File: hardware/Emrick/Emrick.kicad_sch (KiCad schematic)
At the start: 85 parts, among them J1 LED_STRIP_CONNECTOR, J2 UFL, J3 Conn_02x05_Odd_Even, J4 BATT_CONN, P1 USB_C_Plug_USB2.0, Q1 Q_NPN_DGS, Q2 Q_NPN_DGS, Q3 Q_NPN_DGS, SW1 SW_SPST, SW2 SW_MEC_5E (RESET)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

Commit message: some work on pcb and schematic
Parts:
- added C13: ?, Capacitor_SMD:C_0402_1005Metric, symbol Device:C
- added L9: ?, Inductor_SMD:L_0402_1005Metric, symbol Device:L
- C12: value 100pF -> ?
- SW1: footprint Connector_PinHeader_2.54mm:PinHeader_1x03_P2.54mm_Vertical -> switch:SW-TH_3P-P4.70_L11.1-W12.7
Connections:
- net GND: now also C13.2, L9.2
- net at C17.1, L6.2: now also C13.1, L9.1
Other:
- note added: "C17, C13, L9, L6 for antenna matching"
- moved on the sheet: AE1, C17
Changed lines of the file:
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@@
   (junction (at 130.81 93.98) (diameter 0) (color 0 0 0 0)
   )
+  (junction (at 311.15 118.11) (diameter 0) (color 0 0 0 0)
+  )
   (junction (at 118.11 93.98) (diameter 0) (color 0 0 0 0)
   )
@@
   (junction (at 240.03 121.92) (diameter 0) (color 0 0 0 0)
   )
+  (junction (at 320.04 118.11) (diameter 0) (color 0 0 0 0)
+  )
   (junction (at 232.41 114.3) (diameter 0) (color 0 0 0 0)
   )
@@
     (stroke (width 0) (type default) (color 0 0 0 0))
   )
+  (wire (pts (xy 320.04 118.11) (xy 322.58 118.11))
+    (stroke (width 0) (type default) (color 0 0 0 0))
+  )
   (wire (pts (xy 153.67 228.6) (xy 156.21 228.6))
     (stroke (width 0) (type default) (color 0 0 0 0))
@@
     (stroke (width 0) (type default) (color 0 0 0 0))
   )
+  (wire (pts (xy 320.04 121.92) (xy 320.04 118.11))
+    (stroke (width 0) (type default) (color 0 0 0 0))
+  )
   (wire (pts (xy 377.19 220.98) (xy 377.19 222.25))
     (stroke (width 0) (type default) (color 0 0 0 0))
@@
     (stroke (width 0) (type default) (color 0 0 0 0))
   )
+  (wire (pts (xy 311.15 121.92) (xy 311.15 118.11))
+    (stroke (width 0) (type default) (color 0 0 0 0))
+  )
   (wire (pts (xy 153.67 102.87) (xy 153.67 104.14))
     (stroke (width 0) (type default) (color 0 0 0 0))
@@
     (stroke (width 0) (type default) (color 0 0 0 0))
   )
-  (wire (pts (xy 308.61 118.11) (xy 313.69 118.11))
+  (wire (pts (xy 308.61 118.11) (xy 311.15 118.11))
     (stroke (width 0) (type default) (color 0 0 0 0))
   )
@@
     (stroke (width 0) (type default) (color 0 0 0 0))
   )
+  (wire (pts (xy 311.15 118.11) (xy 320.04 118.11))
+    (stroke (width 0) (type default) (color 0 0 0 0))
+  )
   (wire (pts (xy 365.76 215.9) (xy 365.76 219.71))
     (stroke (width 0) (type default) (color 0 0 0 0))
@@
     (stroke (width 0) (type default) (color 0 0 0 0))
   )
-  (wire (pts (xy 321.31 118.11) (xy 330.2 118.11))
+  (wire (pts (xy 330.2 118.11) (xy 339.09 118.11))
     (stroke (width 0) (type default) (color 0 0 0 0))
   )
@@
     (effects (font (size 2 2)) (justify left bottom))
   )
+  (text "C17, C13, L9, L6 for antenna matching" (at 299.72 140.97 0)
+    (effects (font (size 1.27 1.27)) (justify left bottom))
+  )
   (text "Programmable Power/Status LED\n" (at 85.09 20.32 0)
     (effects (font (size 1.27 1.27)) (justify left bottom))
@@
     (property "Reference" "SW1" (id 0) (at 90.17 187.96 0))
     (property "Value" "SW_SPST" (id 1) (at 88.9 190.5 0))
-    (property "Footprint" "Connector_PinHeader_2.54mm:PinHeader_1x03_P2.54mm_Vertical" (id 2) (at 102.87 185.42 0)
+    (property "Footprint" "switch:SW-TH_3P-P4.70_L11.1-W12.7" (id 2) (at 102.87 185.42 0)
       (effects (font (size 1.27 1.27)) hide)
     )
@@
     (pin "2")
   )
+  (symbol (lib_id "Device:L") (at 320.04 125.73 0) (unit 1)
+    (in_bom yes) (on_board yes) (fields_autoplaced)
+    (property "Reference" "L9" (id 0) (at 321.31 124.4599 0)
+      (effects (font (size 1.27 1.27)) (justify left))
+    )
+    (property "Value" "?" (id 1) (at 321.31 126.9999 0)
+      (effects (font (size 1.27 1.27)) (justify left))
+    )
+    (property "Footprint" "Inductor_SMD:L_0402_1005Metric" (id 2) (at 320.04 125.73 0)
+      (effects (font (size 1.27 1.27)) hide)
+    )
+    (property "Datasheet" "~" (id 3) (at 320.04 125.73 0)
+      (effects (font (size 1.27 1.27)) hide)
+    )
+    (pin "1")
+    (pin "2")
+  )
   (symbol (lib_id "power:GND") (at 151.13 274.32 0) (unit 1)
     (in_bom yes) (on_board yes) (fields_autoplaced)
@@
       (effects (font (size 1.27 1.27)) (justify left))
     )
-    (property "Value" "100pF" (id 1) (at 276.86 106.68 0)
+    (property "Value" "?" (id 1) (at 279.4 106.68 0)
       (effects (font (size 1.27 1.27)) (justify left))
     )
@@
     (pin "1")
   )
+  (symbol (lib_id "Device:C") (at 311.15 125.73 0) (unit 1)
+    (in_bom yes) (on_board yes) (fields_autoplaced)
+    (property "Reference" "C13" (id 0) (at 314.96 124.4599 0)
+      (effects (font (size 1.27 1.27)) (justify left))
+    )
+    (property "Value" "?" (id 1) (at 314.96 126.9999 0)
+      (effects (font (size 1.27 1.27)) (justify left))
+    )
+    (property "Footprint" "Capacitor_SMD:C_0402_1005Metric" (id 2) (at 312.1152 129.54 0)
+      (effects (font (size 1.27 1.27)) hide)
+    )
+    (property "Datasheet" "~" (id 3) (at 311.15 125.73 0)
+      (effects (font (size 1.27 1.27)) hide)
+    )
+    (pin "1")
+    (pin "2")
+  )
   (symbol (lib_id "Device:R") (at 284.48 255.27 90) (unit 1)
     (in_bom yes) (on_board yes)
@@
     (pin "1")
   )
-  (symbol (lib_id "Device:Antenna") (at 330.2 113.03 0) (unit 1)
+  (symbol (lib_id "Device:Antenna") (at 339.09 113.03 0) (unit 1)
     (in_bom yes) (on_board yes) (fields_autoplaced)
-    (property "Reference" "AE1" (id 0) (at 332.74 112.3949 0)
+    (property "Reference" "AE1" (id 0) (at 341.63 112.3949 0)
       (effects (font (size 1.27 1.27)) (justify left))
     )
-    (property "Value" "Antenna" (id 1) (at 332.74 114.9349 0)
+    (property "Value" "Antenna" (id 1) (at 341.63 114.9349 0)
       (effects (font (size 1.27 1.27)) (justify left))
     )
-    (property "Footprint" "Emrick Footprints:emrick_custom_antenna" (id 2) (at 330.2 113.03 0)
+    (property "Footprint" "Emrick Footprints:emrick_custom_antenna" (id 2) (at 339.09 113.03 0)
       (effects (font (size 1.27 1.27)) hide)
     )
-    (property "Datasheet" "~" (id 3) (at 330.2 113.03 0)
+    (property "Datasheet" "~" (id 3) (at 339.09 113.03 0)
       (effects (font (size 1.27 1.27)) hide)
     )
@@
       (effects (font (size 1.524 1.524)) hide)
     )
-    (property "Datasheet" "" (id 3) (at 356.87 218.44 0)
+    (property "Datasheet" "https://www.ti.com/lit/ds/symlink/tps63020.pdf" (id 3) (at 349.25 175.26 0)
       (effects (font (size 1.524 1.524)))
     )
@@
     (pin "2")
   )
-  (symbol (lib_id "Device:C") (at 317.5 118.11 90) (unit 1)
+  (symbol (lib_id "Device:C") (at 326.39 118.11 90) (unit 1)
     (in_bom yes) (on_board yes) (fields_autoplaced)
-    (property "Reference" "C17" (id 0) (at 317.5 110.49 90))
-    (property "Value" "5.6pF" (id 1) (at 317.5 113.03 90))
-    (property "Footprint" "Capacitor_SMD:C_0402_1005Metric" (id 2) (at 321.31 117.1448 0)
+    (property "Reference" "C17" (id 0) (at 326.39 110.49 90))
+    (property "Value" "5.6pF" (id 1) (at 326.39 113.03 90))
+    (property "Footprint" "Capacitor_SMD:C_0402_1005Metric" (id 2) (at 330.2 117.1448 0)
       (effects (font (size 1.27 1.27)) hide)
     )
-    (property "Datasheet" "~" (id 3) (at 317.5 118.11 0)
+    (property "Datasheet" "~" (id 3) (at 326.39 118.11 0)
       (effects (font (size 1.27 1.27)) hide)
     )
@@
     (pin "2")
   )
+  (symbol (lib_id "power:GND") (at 311.15 129.54 0) (unit 1)
+    (in_bom yes) (on_board yes) (fields_autoplaced)
+    (property "Reference" "#PWR016" (id 0) (at 311.15 135.89 0)
+      (effects (font (size 1.27 1.27)) hide)
+    )
+    (property "Value" "GND" (id 1) (at 311.15 134.62 0))
+    (property "Footprint" "" (id 2) (at 311.15 129.54 0)
+      (effects (font (size 1.27 1.27)) hide)
+    )
+    (property "Datasheet" "" (id 3) (at 311.15 129.54 0)
+      (effects (font (size 1.27 1.27)) hide)
+    )
+    (pin "1")
+  )
   (symbol (lib_id "Device:C") (at 259.08 125.73 0) (unit 1)
     (in_bom yes) (on_board yes) (fields_autoplaced)
@@
     (pin "1")
   )
+  (symbol (lib_id "power:GND") (at 320.04 129.54 0) (unit 1)
+    (in_bom yes) (on_board yes) (fields_autoplaced)
+    (property "Reference" "#PWR049" (id 0) (at 320.04 135.89 0)
+      (effects (font (size 1.27 1.27)) hide)
+    )
+    (property "Value" "GND" (id 1) (at 320.04 134.62 0))
+    (property "Footprint" "" (id 2) (at 320.04 129.54 0)
+      (effects (font (size 1.27 1.27)) hide)
+    )
+    (property "Datasheet" "" (id 3) (at 320.04 129.54 0)
+      (effects (font (size 1.27 1.27)) hide)
+    )
+    (pin "1")
+  )
   (symbol (lib_id "Device:R") (at 31.75 238.76 0) (unit 1)
     (in_bom yes) (on_board yes) (fields_autoplaced)
@@
       (reference "#PWR015") (unit 1) (value "GND") (footprint "")
     )
+    (path "/c4a0c265-4b39-41d3-ab53-2ab4874fa3fe"
+      (reference "#PWR016") (unit 1) (value "GND") (footprint "")
+    )
     (path "/1114404f-4690-4e3f-9b08-e30201bf3fb3"
       (reference "#PWR017") (unit 1) (value "GND") (footprint "")
@@
       (reference "#PWR048") (unit 1) (value "GND") (footprint "")
     )
+    (path "/eaf0c0f4-f8ef-48ee-830b-828643b639bd"
+      (reference "#PWR049") (unit 1) (value "GND") (footprint "")
+    )
     (path "/d7b546ac-1aeb-4e32-be9e-b8ba6b0d2d70"
       (reference "#PWR050") (unit 1) (value "GND") (footprint "")
@@
     )
     (path "/4f3938ec-ee10-4033-b043-17e527f7cafe"
-      (reference "C12") (unit 1) (value "100pF") (footprint "Capacitor_SMD:C_0402_1005Metric")
+      (reference "C12") (unit 1) (value "?") (footprint "Capacitor_SMD:C_0402_1005Metric")
+    )
+    (path "/50c8f597-eecd-41b3-b369-057fd39f4039"
+      (reference "C13") (unit 1) (value "?") (footprint "Capacitor_SMD:C_0402_1005Metric")
     )
     (path "/131a06d2-a108-46d7-83da-eec9c5e5b8d7"
@@
       (reference "L8") (unit 1) (value "1.5uH") (footprint "Inductor_SMD:L_Sunlord_MWSA0518_5.4x5.2mm")
     )
+    (path "/3240c5b7-b3f1-4039-96ce-b8816fd0780e"
+      (reference "L9") (unit 1) (value "?") (footprint "Inductor_SMD:L_0402_1005Metric")
+    )
     (path "/98b2397c-2d8e-4422-bb18-42d4b4daae2e"
       (reference "P1") (unit 1) (value "USB_C_Plug_USB2.0") (footprint "Connector_USB:USB_C_Receptacle_XKB_U262-16XN-4BVC11")
@@
     )
     (path "/296a890d-93e3-479a-910f-fa1bd31332ae"
-      (reference "SW1") (unit 1) (value "SW_SPST") (footprint "Connector_PinHeader_2.54mm:PinHeader_1x03_P2.54mm_Vertical")
+      (reference "SW1") (unit 1) (value "SW_SPST") (footprint "switch:SW-TH_3P-P4.70_L11.1-W12.7")
     )
     (path "/b30242dc-8228-402b-8e4f-fd03a02393d4"

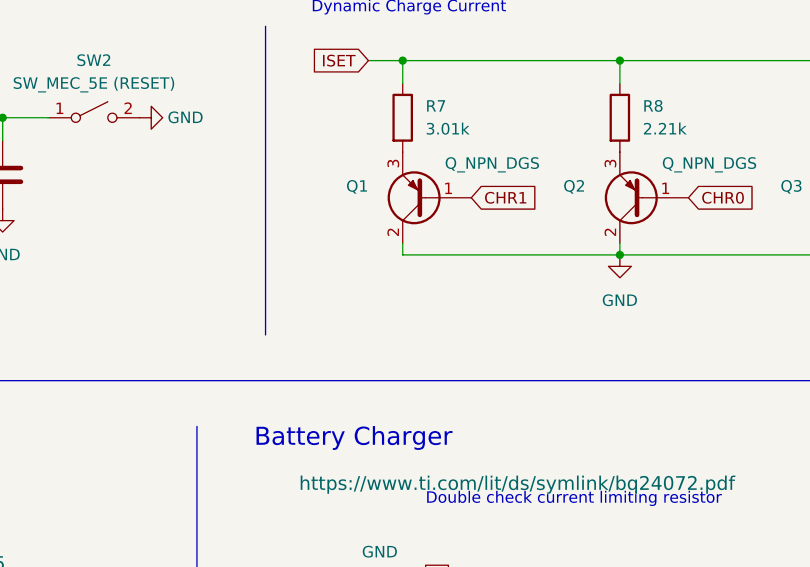
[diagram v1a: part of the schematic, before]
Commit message: add correct nmos symbol (but just add it, not actually hook it up or anything
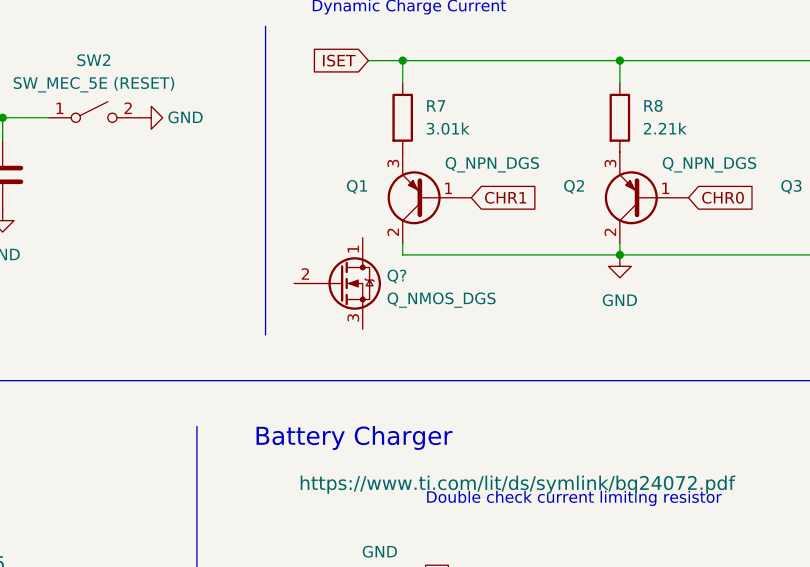
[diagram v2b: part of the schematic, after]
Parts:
- added Q?: Q_NMOS_DGS, symbol Device:Q_NMOS_DGS
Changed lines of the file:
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@@
     (pin "2")
+  )
+  (symbol (lib_id "Device:Q_NMOS_DGS") (at 213.995 200.025 0) (unit 1)
+    (in_bom yes) (on_board yes) (fields_autoplaced)
+    (property "Reference" "Q?" (id 0) (at 219.202 199.1903 0)
+      (effects (font (size 1.27 1.27)) (justify left))
+    )
+    (property "Value" "Q_NMOS_DGS" (id 1) (at 219.202 201.7272 0)
+      (effects (font (size 1.27 1.27)) (justify left))
+    )
+    (property "Footprint" "" (id 2) (at 219.075 197.485 0)
+      (effects (font (size 1.27 1.27)) hide)
+    )
+    (property "Datasheet" "~" (id 3) (at 213.995 200.025 0)
+      (effects (font (size 1.27 1.27)) hide)
+    )
+    (pin "1")
+    (pin "2")
+    (pin "3")
   )
   (symbol (lib_id "Device:LED") (at 106.68 34.29 0) (unit 1)
@@
       (reference "Q3") (unit 1) (value "Q_NPN_DGS") (footprint "Emrick Footprints:DTC143ZMT2L")
     )
+    (path "/cb06ee6c-4b12-4bdb-8820-222eef2ada64"
+      (reference "Q?") (unit 1) (value "Q_NMOS_DGS") (footprint "")
+    )
     (path "/7c976042-82e8-4bec-9beb-b8a292d80d1c"

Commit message: updated schematic
replaced BJTs with nMOSFETs, set power supply of B/B regulator and VREGIN of USB chip to CHG_OUT (battery charger output)
STILL NEED:
A way to disable B/B regulator
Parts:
- removed D5: S2A, Emrick Footprints:PMEG120G20ELRX, symbol pspice:DIODE
- removed Q1, Q2, Q3: Q_NPN_DGS, Emrick Footprints:DTC143ZMT2L, symbol Transistor_BJT:BCX53
- added Q? (x2): Q_NMOS_DGS, symbol Device:Q_NMOS_DGS
- C27, C28: value 22uF -> 10uF
- C29: value 2uF -> 10uF
- L8: value 1.5uH -> 1uH
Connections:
- net CHR0: now also Q?.2 (G)
- net CHR1: now also Q?.2 (G)
- net CHREN: now also Q?.2 (G)
- net GND: now also Q?.3 (S), Q?.3 (S), Q?.3 (S)
- net VBAT: no longer C25.2, C26.2, U3.10 (VIN), U3.11 (VIN), U3.12 (EN), U4.7 (VREGIN)
- net at R9.2: now also Q?.1 (D)
- net CHG_OUT: now reaches U6.10 (OUT)
- net CHG_OUT: now also C25.2, C26.2, U3.10 (VIN), U3.11 (VIN), U4.7 (VREGIN), U6.11 (OUT)
- net at R8.2: now also Q?.1 (D)
- net at R7.2: now also Q?.1 (D)
- new net ???: U3.12 (EN)
- no-connect marks 39 -> 37
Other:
- moved on the sheet: C25, C26, C27, C28, C29, C30, L8, Q?, R10, R11, R12, U3

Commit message: Update schematic with rev 2 changes
Add extra capacitors to power pins on CP2102N
Add boost enable pin to micro
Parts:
- removed R21, R3: 0, Resistor_SMD:R_0402_1005Metric, symbol Device:R
- added C14, C34: 4.7uF, Capacitor_SMD:C_0402_1005Metric, symbol Device:C
- added C35, C36: .1uF, Capacitor_SMD:C_0402_1005Metric, symbol Device:C
- C12, C13: footprint Capacitor_SMD:C_0402_1005Metric -> Capacitor_SMD:C_0201_0603Metric
- gave numbers to parts that had none: 3
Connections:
- net ??? is gone; now on net BOOST_ENABLE: U3.12 (EN)
- net CHG_OUT: now also C14.1, C35.1
- net GND: now also C14.2, C34.2, C35.2, C36.2
- net VDDS: now also C34.1, C36.1
- net WMCU_VDDS: now also C32.1, J3.1 (Pin_1), U5.8 (VCC)
- net BOOST_ENABLE: now reaches U2.29 (DIO_19)
- no-connect marks 37 -> 36
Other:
- note added: "Decoupling capacitors for CP2102N Power Pins"
- note removed: "Assuming VDDS is the right system supply we want to use. Need to double check this stuff and also increase the charge limit"
- note removed: "Double check removed decoupling caps on VDD and VREGIN!"
